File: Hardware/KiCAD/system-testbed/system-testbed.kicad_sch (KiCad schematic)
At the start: 1 part, among them IC2 PCF8575PWR

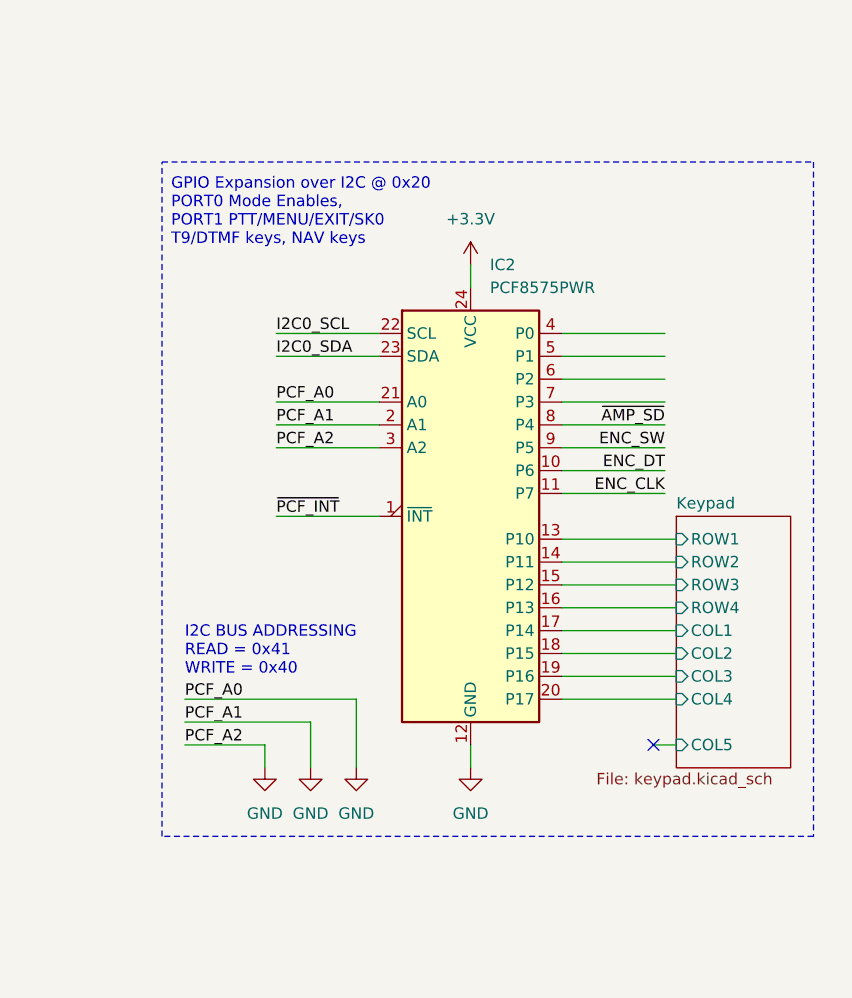
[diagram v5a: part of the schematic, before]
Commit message: fix: move port expander over to HMI schematic #15 #33
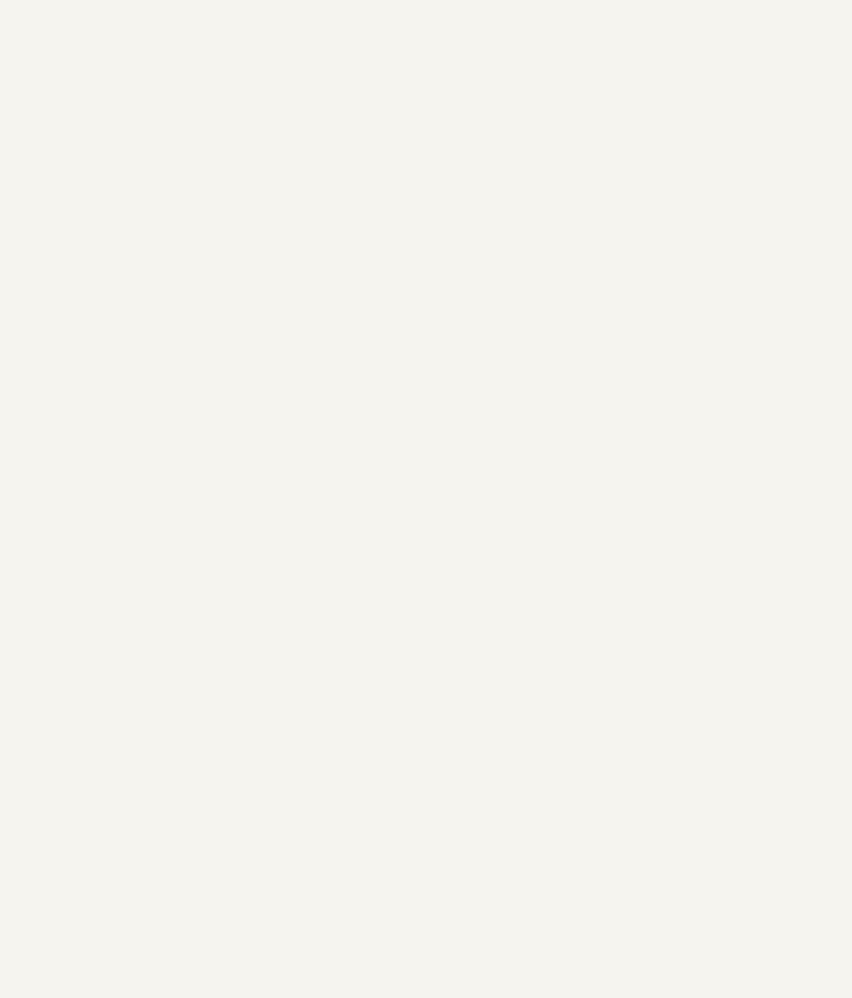
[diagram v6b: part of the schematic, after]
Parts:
- removed IC2: PCF8575PWR, Package_SO:SSOP-24_5.3x8.2mm_P0.65mm, symbol Interface_Expansion:PCF8575DBR
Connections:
- no-connect marks 1 -> 0
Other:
- removed sheet Keypad
- note removed: "GPIO Expansion over I2C @ 0x20 PORT0 Mode Enables, PORT1 PTT/MENU/EXIT/SK0 T9/DTMF keys, NAV keys"
- note removed: "I2C BUS ADDRESSING READ = 0x41 WRITE = 0x40"

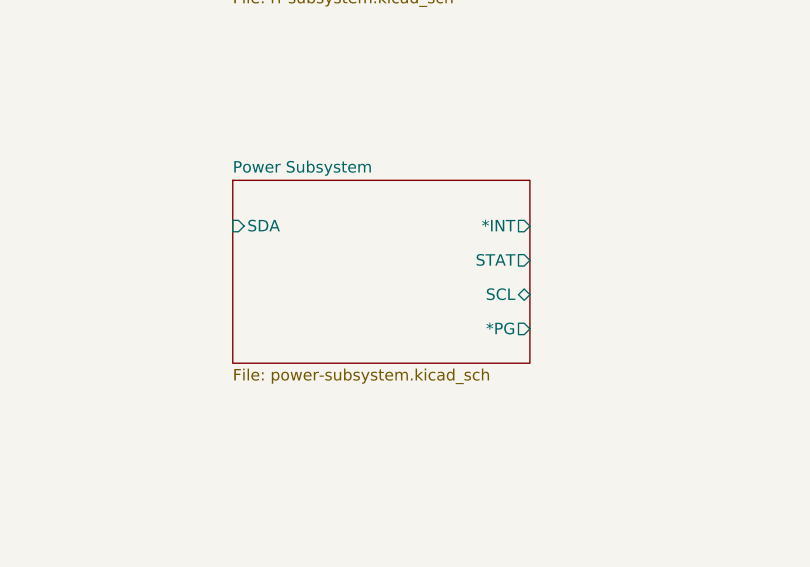
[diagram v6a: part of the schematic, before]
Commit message: feat: Update to PSU Power Supply PCB Fixes #31
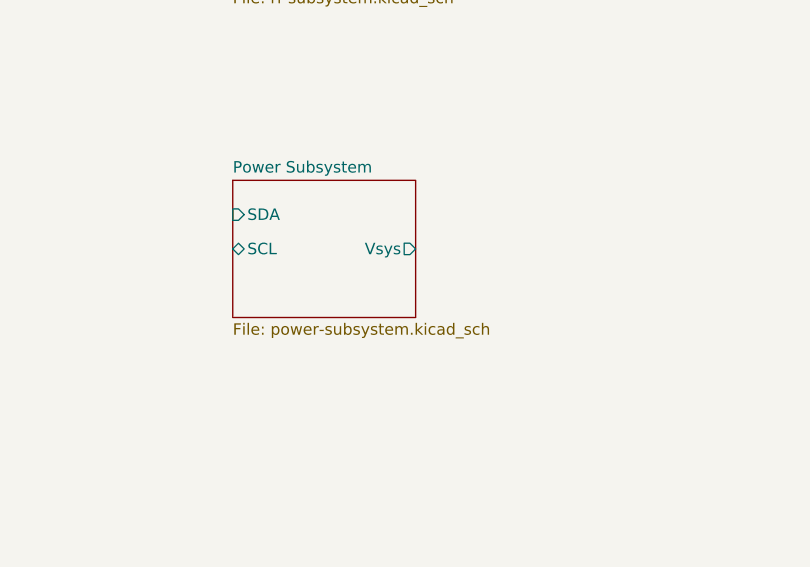
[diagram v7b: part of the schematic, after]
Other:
- sheet Power Subsystem ports: added Vsys; removed *INT, *PG, STAT
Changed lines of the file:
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@@
 	(sheet
 		(at 125.73 139.7)
-		(size 33.02 20.32)
+		(size 20.32 15.24)
 		(exclude_from_sim no)
 		(in_bom yes)
@@
 		)
 		(property "Sheetfile" "power-subsystem.kicad_sch"
-			(at 125.73 160.6046 0)
+			(at 125.73 155.5246 0)
 			(effects
 				(font
@@
 			)
 		)
-		(pin "*INT" output
-			(at 158.75 144.78 0)
+		(pin "Vsys" output
+			(at 146.05 147.32 0)
 			(effects
 				(font
@@
 		)
 		(pin "SDA" input
-			(at 125.73 144.78 180)
+			(at 125.73 143.51 180)
 			(effects
 				(font
@@
 			)
 		)
-		(pin "STAT" output
-			(at 158.75 148.59 0)
+		(pin "SCL" bidirectional
+			(at 125.73 147.32 180)
 			(effects
 				(font
 					(size 1.27 1.27)
 				)
-				(justify right)
+				(justify left)
 			)
 		)
-		(pin "SCL" bidirectional
-			(at 158.75 152.4 0)
-			(effects
-				(font
-					(size 1.27 1.27)
-				)
-				(justify right)
-			)
-		)
-		(pin "*PG" output
-			(at 158.75 156.21 0)
-			(effects
-				(font
-					(size 1.27 1.27)
-				)
-				(justify right)
-			)
-		)

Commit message: feat: Testing Sync
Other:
- note removed: "THE CUBE"
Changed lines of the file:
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@@
-		)
-	)
-	(text "THE CUBE"
-		(exclude_from_sim no)
-		(at 25.654 187.706 0)
-		(effects
-			(font
-				(size 2.54 2.54)
-				(thickness 0.508)
-				(bold yes)
-			)
 		)
 	)
